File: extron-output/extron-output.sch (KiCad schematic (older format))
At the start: 12 parts, among them J1 SCART-F, J10 Conn_01x01, J11 Conn_01x01, J2 RED, J3 GREEN, J4 BLUE, J5 SYNC, J6 PHOENIX, J8 Conn_01x01, J9 Conn_01x01, SW1 SW_SPDT

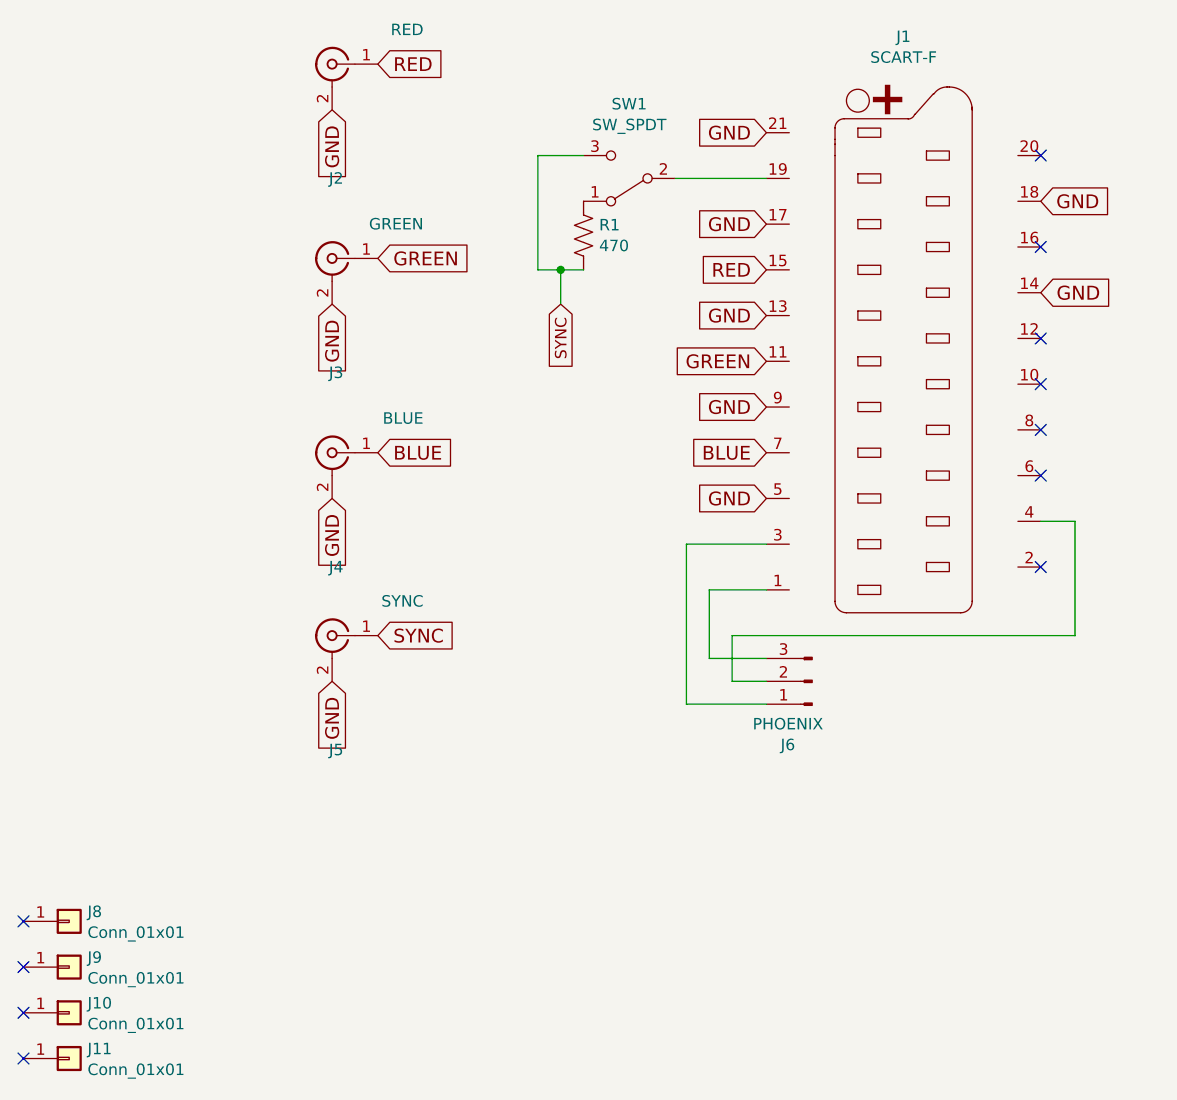
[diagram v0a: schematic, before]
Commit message: Update extron output board to use combined RCA (v2.1)
Small fixes for extron input as well (v2.1)
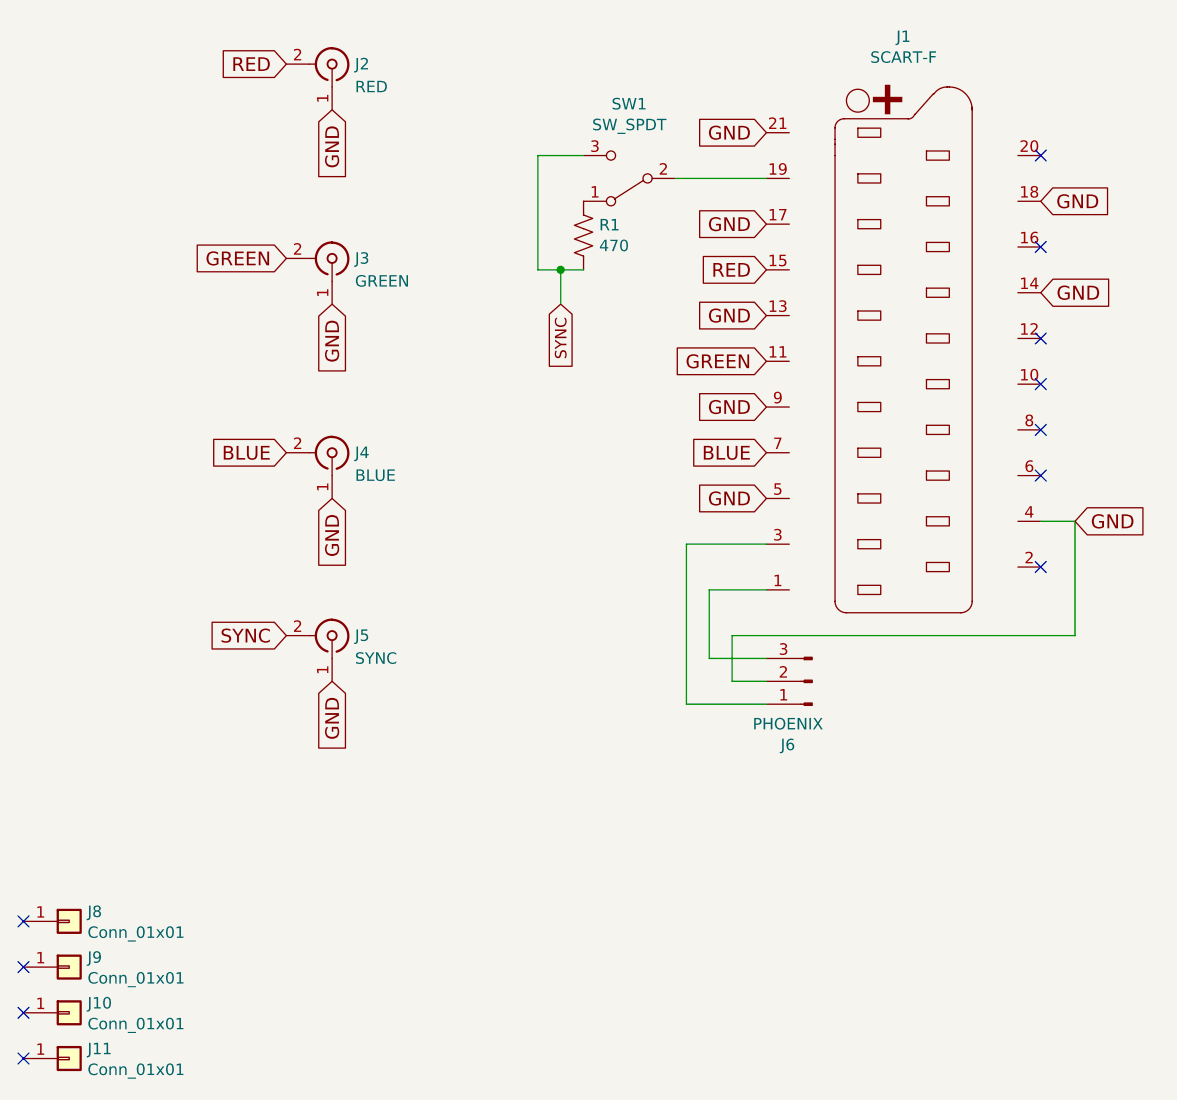
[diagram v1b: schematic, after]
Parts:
- J2, J3, J4, J5: footprint extron-output:BNC_90 -> extron-output:rca_combined
- J6: footprint Connector_JST:JST_EH_S03B-EH_1x03_P2.50mm_Horizontal -> Connector_JST:JST_XH_S3B-XH-A-1_1x03_P2.50mm_Horizontal
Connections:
- net BLUE: now also J4.2 (Ext); no longer J4.1 (In)
- net GND: now also J1.4 (P4), J2.1 (In), J3.1 (In), J4.1 (In), J5.1 (In), J6.2 (Pin_2); no longer J2.2 (Ext), J3.2 (Ext), J4.2 (Ext), J5.2 (Ext)
- net GREEN: now also J3.2 (Ext); no longer J3.1 (In)
- net RED: now also J2.2 (Ext); no longer J2.1 (In)
- net SYNC: now also J5.2 (Ext); no longer J5.1 (In)
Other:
- moved on the sheet: J2, J3, J4, J5
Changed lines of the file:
@@
 LIBS:74xx
 LIBS:extron-output-cache
-EELAYER 26 0
+EELAYER 29 0
 EELAYER END
 $Descr A4 11693 8268
 encoding utf-8
 Sheet 1 1
-Title ""
-Date ""
-Rev ""
-Comp ""
+Title "Extron Scart Adapter (Output)"
+Date "2019-04-13"
+Rev "2.1"
+Comp "Rattboi (Bradon Kanyid)"
 Comment1 ""
 Comment2 ""
@@
 Text GLabel 3750 2050 3    60   Input ~ 0
 GND
-Text GLabel 3950 4350 2    60   Input ~ 0
+Text GLabel 3550 4350 0    60   Input ~ 0
 SYNC
-Text GLabel 3950 3550 2    60   Input ~ 0
+Text GLabel 3550 3550 0    60   Input ~ 0
 BLUE
-Text GLabel 3950 1850 2    60   Input ~ 0
+Text GLabel 3550 1850 0    60   Input ~ 0
 RED
 $Comp
@@
 U 1 1 5C651C5B
 P 3750 1850
-F 0 "J2" H 3700 1350 50  0000 L CNN
-F 1 "RED" H 3350 2000 50  0000 L CNN
-F 2 "extron-output:BNC_90" H 3750 1850 50  0001 C CNN
+F 0 "J2" V 3750 1950 50  0000 L CNN
+F 1 "RED" V 3650 1950 50  0000 L CNN
+F 2 "extron-output:rca_combined" H 3750 1850 50  0001 C CNN
 F 3 " ~" H 3750 1850 50  0001 C CNN
 	1    3750 1850
-	-1   0    0    -1
+	0    1    -1   0
 $EndComp
 $Comp
@@
 U 1 1 5C651D00
 P 3750 2700
-F 0 "J3" H 3700 2200 50  0000 L CNN
-F 1 "GREEN" H 3350 2850 50  0000 L CNN
-F 2 "extron-output:BNC_90" H 3750 2700 50  0001 C CNN
+F 0 "J3" V 3750 2800 50  0000 L CNN
+F 1 "GREEN" V 3650 2800 50  0000 L CNN
+F 2 "extron-output:rca_combined" H 3750 2700 50  0001 C CNN
 F 3 " ~" H 3750 2700 50  0001 C CNN
 	1    3750 2700
-	-1   0    0    -1
+	0    1    -1   0
 $EndComp
 $Comp
@@
 U 1 1 5C651DB2
 P 3750 3550
-F 0 "J4" H 3700 3050 50  0000 L CNN
-F 1 "BLUE" H 3350 3700 50  0000 L CNN
-F 2 "extron-output:BNC_90" H 3750 3550 50  0001 C CNN
+F 0 "J4" V 3750 3650 50  0000 L CNN
+F 1 "BLUE" V 3650 3650 50  0000 L CNN
+F 2 "extron-output:rca_combined" H 3750 3550 50  0001 C CNN
 F 3 " ~" H 3750 3550 50  0001 C CNN
 	1    3750 3550
-	-1   0    0    -1
+	0    1    -1   0
 $EndComp
 $Comp
@@
 U 1 1 5C651E83
 P 3750 4350
-F 0 "J5" H 3700 3850 50  0000 L CNN
-F 1 "SYNC" H 3350 4500 50  0000 L CNN
-F 2 "extron-output:BNC_90" H 3750 4350 50  0001 C CNN
+F 0 "J5" V 3750 4450 50  0000 L CNN
+F 1 "SYNC" V 3650 4450 50  0000 L CNN
+F 2 "extron-output:rca_combined" H 3750 4350 50  0001 C CNN
 F 3 " ~" H 3750 4350 50  0001 C CNN
 	1    3750 4350
-	-1   0    0    -1
+	0    1    -1   0
 $EndComp
 Text GLabel 3750 2900 3    60   Input ~ 0
@@
 F 0 "J6" H 5956 4828 50  0000 C CNN
 F 1 "PHOENIX" H 5956 4737 50  0000 C CNN
-F 2 "Connector_JST:JST_EH_S03B-EH_1x03_P2.50mm_Horizontal" H 5850 4550 50  0001 C CNN
+F 2 "Connector_JST:JST_XH_S3B-XH-A-1_1x03_P2.50mm_Horizontal" H 5850 4550 50  0001 C CNN
 F 3 "~" H 5850 4550 50  0001 C CNN
 	1    5850 4550
@@
 	1    0    0    -1
 $EndComp
-Text GLabel 3950 2700 2    60   Input ~ 0
+Text GLabel 3550 2700 0    60   Input ~ 0
 GREEN
 NoConn ~ 6850 4050
@@
 Text GLabel 4750 2900 3    50   Input ~ 0
 SYNC
+Text GLabel 7000 3850 2    61   Input ~ 0
+GND
 $EndSCHEMATC
